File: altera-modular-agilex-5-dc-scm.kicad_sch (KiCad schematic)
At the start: 6 parts

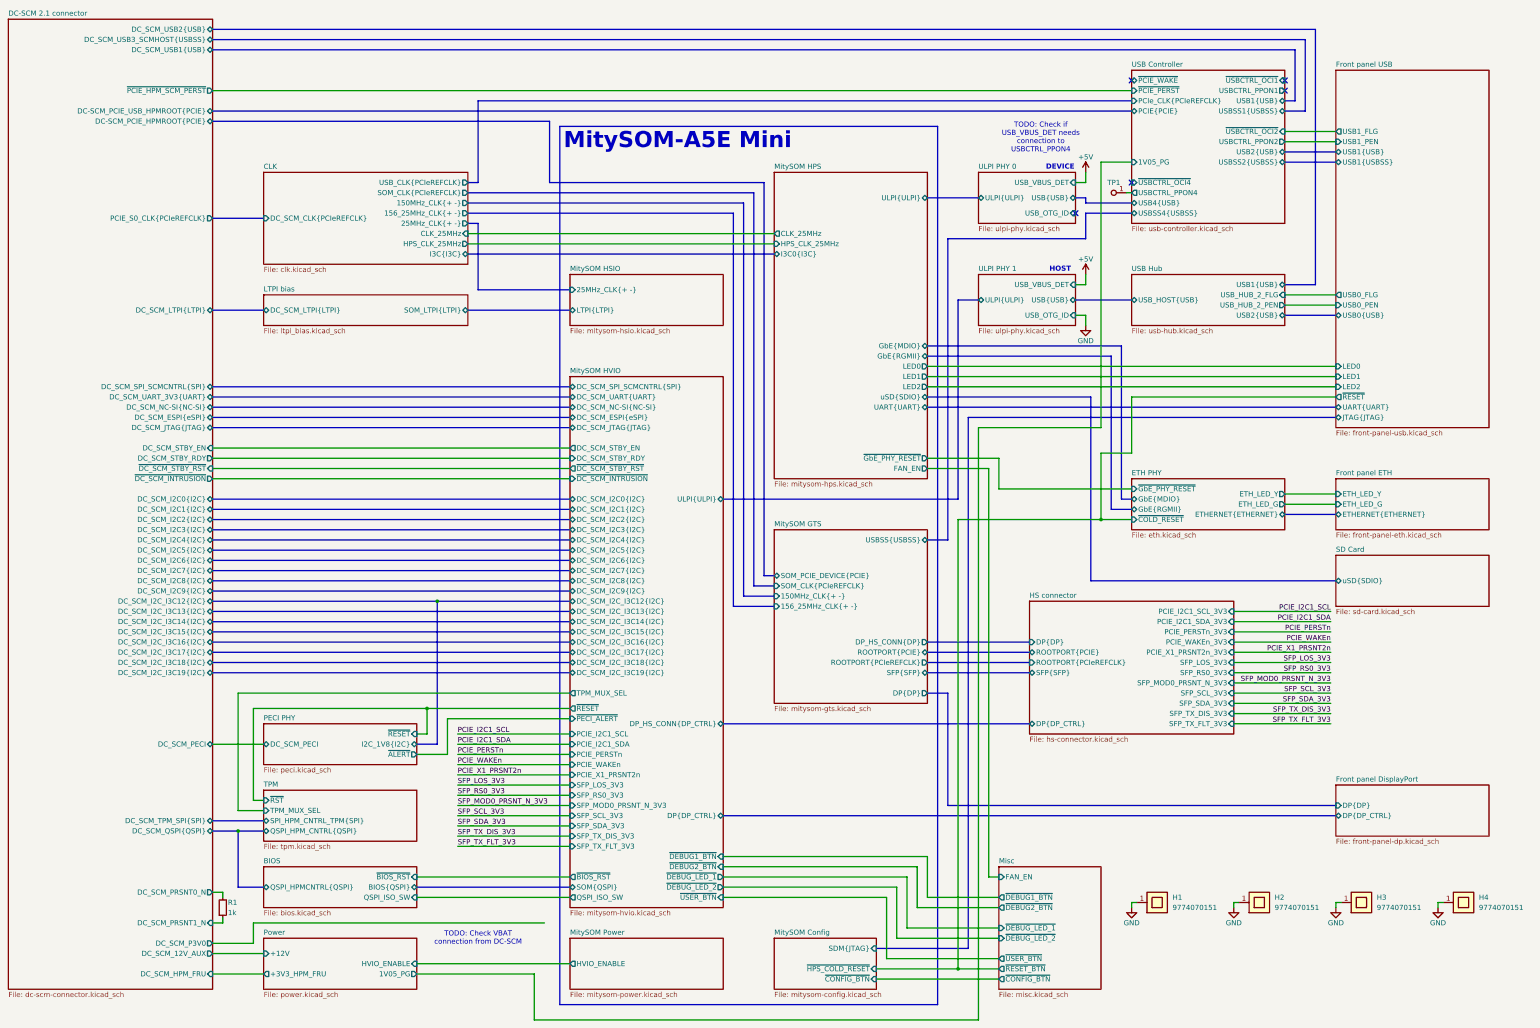
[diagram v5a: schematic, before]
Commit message: [#100595] Update connections according to client request
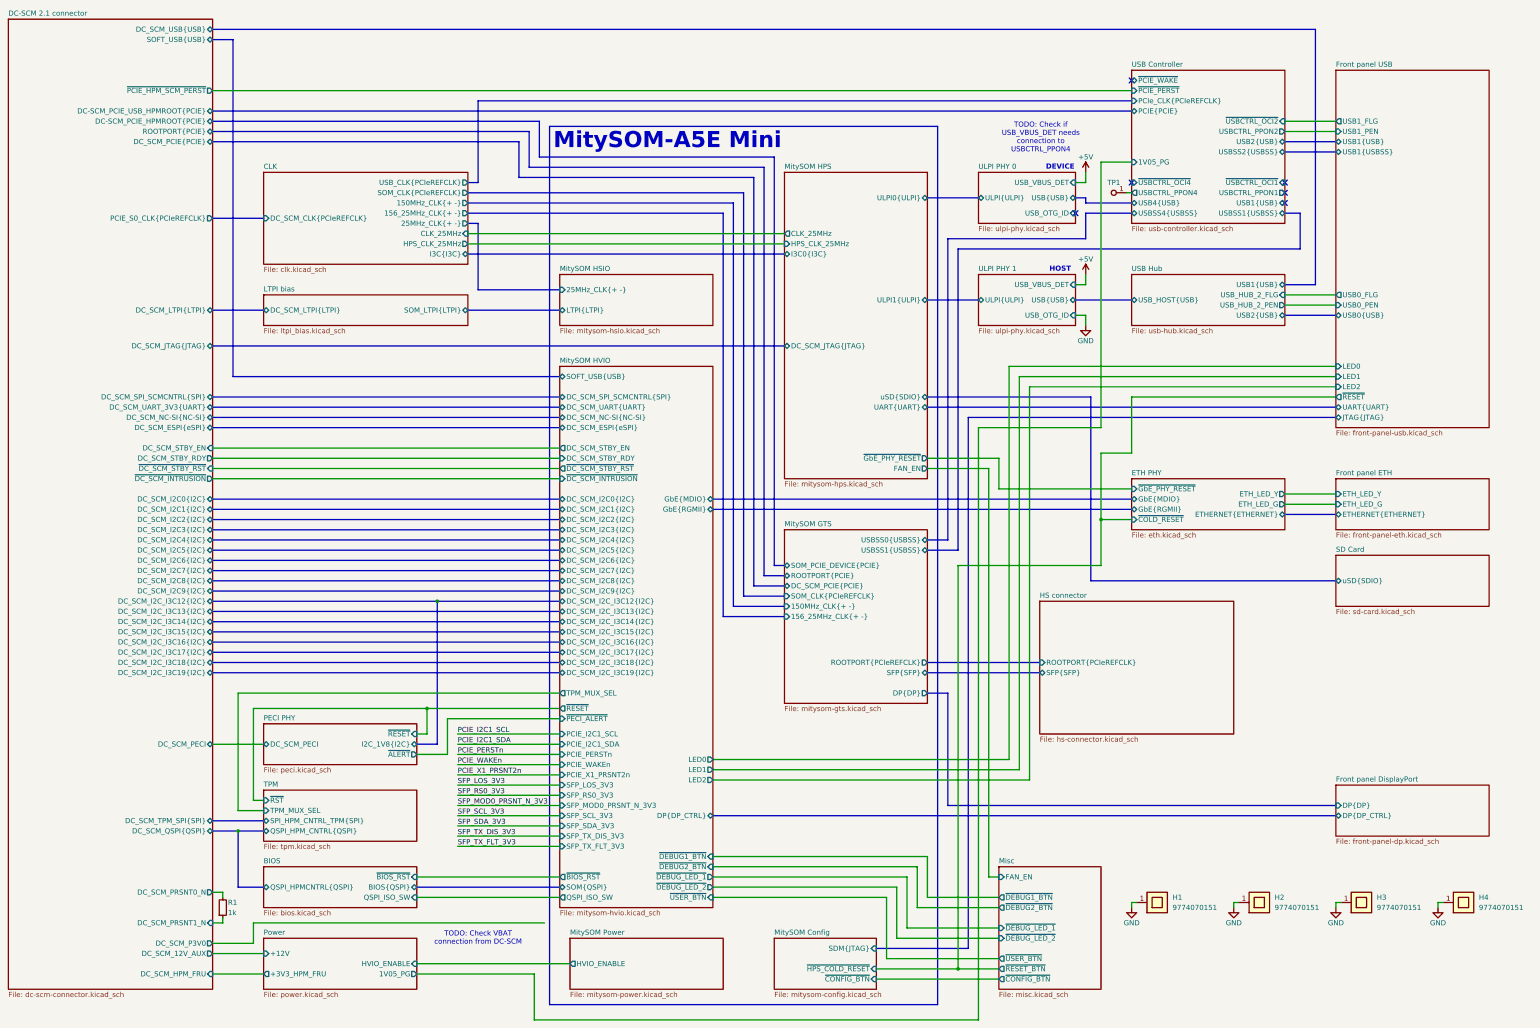
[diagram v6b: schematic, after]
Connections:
- no-connect marks 5 -> 6
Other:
- sheet DC-SCM 2.1 connector ports: added DC_SCM_PCIE{PCIE}, DC_SCM_USB{USB}, ROOTPORT{PCIE}, SOFT_USB{USB}; removed DC_SCM_USB1{USB}, DC_SCM_USB2{USB}, DC_SCM_USB3_SCMHOST{USBSS}
- sheet HS connector ports: added none; removed DP{DP_CTRL}, DP{DP}, PCIE_I2C1_SCL_3V3, PCIE_I2C1_SDA_3V3, PCIE_PERSTn_3V3, PCIE_WAKEn_3V3, PCIE_X1_PRSNT2n_3V3, ROOTPORT{PCIE}, SFP_LOS_3V3, SFP_MOD0_PRSNT_N_3V3, SFP_RS0_3V3, SFP_SCL_3V3, SFP_SDA_3V3, SFP_TX_DIS_3V3, SFP_TX_FLT_3V3
- sheet MitySOM GTS ports: added DC_SCM_PCIE{PCIE}, USBSS0{USBSS}, USBSS1{USBSS}; removed DP_HS_CONN{DP}, USBSS{USBSS}
- sheet MitySOM HPS ports: added DC_SCM_JTAG{JTAG}, ULPI0{ULPI}, ULPI1{ULPI}; removed GbE{MDIO}, GbE{RGMII}, LED0, LED1, LED2, ULPI{ULPI}
- sheet MitySOM HVIO ports: added GbE{MDIO}, GbE{RGMII}, LED0, LED1, LED2, SOFT_USB{USB}; removed DC_SCM_JTAG{JTAG}, DP_HS_CONN{DP_CTRL}, ULPI{ULPI}

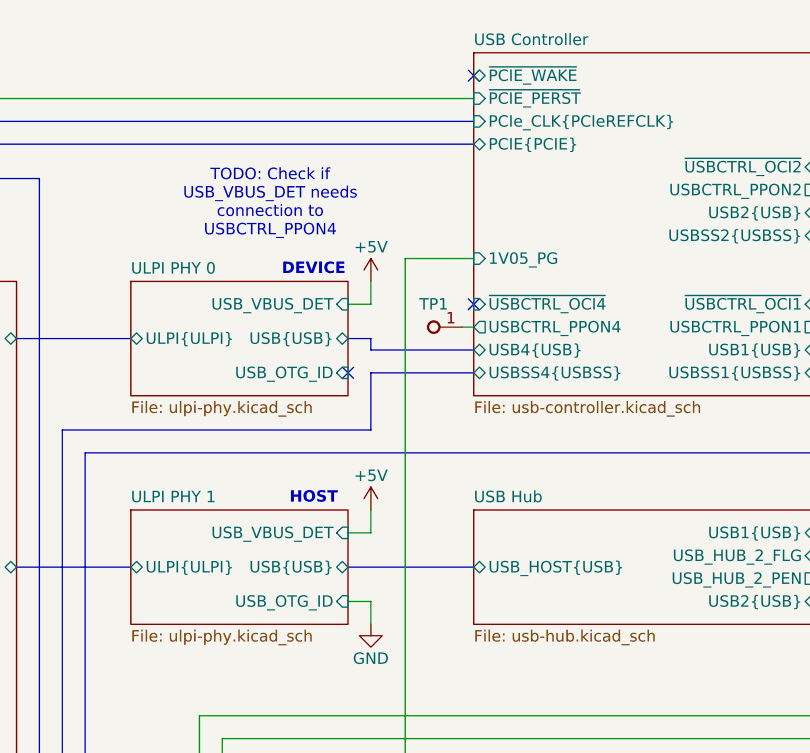
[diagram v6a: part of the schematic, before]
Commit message: [#100501] Connect ULPI CPEN signal to USB hub VBUS_DET
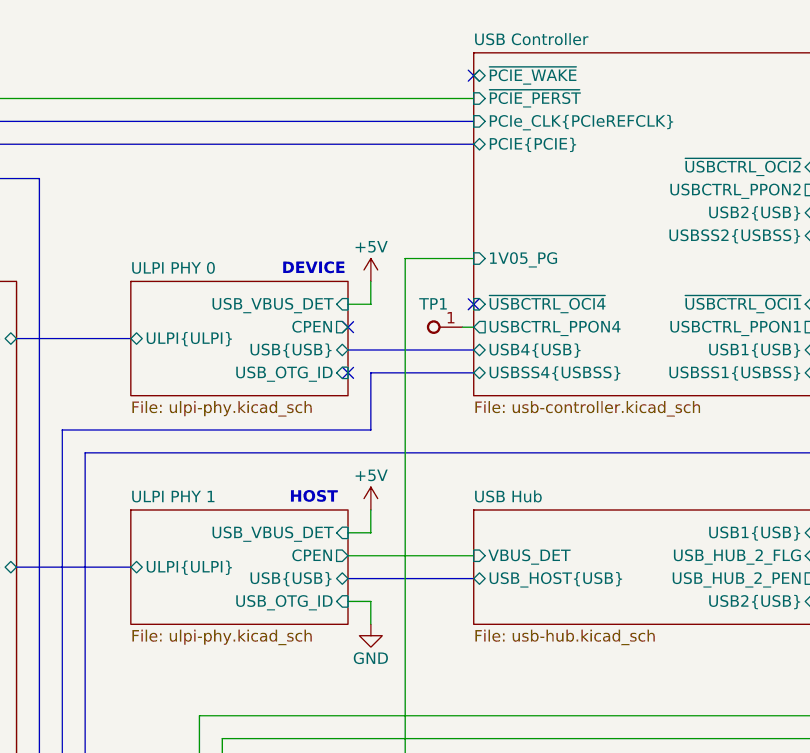
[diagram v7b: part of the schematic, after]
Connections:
- no-connect marks 6 -> 7
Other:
- sheet ULPI PHY 0 ports: added CPEN; removed none
- sheet ULPI PHY 1 ports: added CPEN; removed none
- sheet USB Hub ports: added VBUS_DET; removed none
- note removed: "TODO: Check if USB_VBUS_DET needs connection to USBCTRL_PPON4"
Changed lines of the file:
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@@
 		(company "Altera")
 	)
-	(text "TODO: Check if\nUSB_VBUS_DET needs\nconnection to\nUSBCTRL_PPON4"
-		(exclude_from_sim no)
-		(at 282.194 54.864 0)
-		(effects
-			(font
-				(size 1.27 1.27)
-			)
-		)
-	)
 	(text "HOST"
 		(exclude_from_sim no)
@@
 	)
 	(no_connect
+		(at 290.83 68.58)
+	)
+	(no_connect
 		(at 304.8 40.64)
 	)
@@
 	(bus
 		(pts
-			(xy 290.83 69.85) (xy 293.37 69.85)
+			(xy 290.83 71.12) (xy 304.8 71.12)
 		)
 		(stroke
@@
 	(wire
 		(pts
+			(xy 290.83 93.98) (xy 304.8 93.98)
+		)
+		(stroke
+			(width 0)
+			(type default)
+		)
+	)
+	(wire
+		(pts
 			(xy 261.62 261.62) (xy 271.78 261.62)
 		)
@@
 	(bus
 		(pts
-			(xy 304.8 71.12) (xy 293.37 71.12)
-		)
-		(stroke
-			(width 0)
-			(type default)
-		)
-	)
-	(bus
-		(pts
-			(xy 290.83 95.25) (xy 304.8 95.25)
+			(xy 290.83 96.52) (xy 304.8 96.52)
 		)
 		(stroke
@@
 		)
 	)
-	(bus
-		(pts
-			(xy 293.37 71.12) (xy 293.37 69.85)
-		)
-		(stroke
-			(width 0)
-			(type default)
-		)
-	)
 	(wire
 		(pts
@@
 		)
 		(pin "USB_HOST{USB}" bidirectional
-			(at 304.8 95.25 180)
+			(at 304.8 96.52 180)
 			(effects
 				(font
@@
 			)
 		)
+		(pin "VBUS_DET" input
+			(at 304.8 93.98 180)
+			(effects
+				(font
+					(size 1.27 1.27)
+				)
+				(justify left)
+			)
+		)
 		(instances
 			(project "altera-modular-agilex-5-dc-scm"
@@
 		)
 		(pin "USB{USB}" bidirectional
-			(at 290.83 69.85 0)
+			(at 290.83 71.12 0)
+			(effects
+				(font
+					(size 1.27 1.27)
+				)
+				(justify right)
+			)
+		)
+		(pin "CPEN" output
+			(at 290.83 68.58 0)
 			(effects
 				(font
@@
 		)
 		(pin "USB{USB}" bidirectional
-			(at 290.83 95.25 0)
+			(at 290.83 96.52 0)
+			(effects
+				(font
+					(size 1.27 1.27)
+				)
+				(justify right)
+			)
+		)
+		(pin "CPEN" output
+			(at 290.83 93.98 0)
 			(effects
 				(font

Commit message: [#100595] Update HS connections
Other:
- sheet HS connector ports: added PCIE_CLKREQ_N, PCIE_DET_WAKE, PCIE_PWR_EN, PCIE_RST_B; removed none
- sheet MitySOM HVIO ports: added PCIE_CLKREQ_N, PCIE_DET_WAKE, PCIE_PWR_EN, PCIE_RST_B; removed PCIE_I2C1_SCL, PCIE_I2C1_SDA, PCIE_PERSTn, PCIE_WAKEn, PCIE_X1_PRSNT2n, SFP_LOS_3V3, SFP_MOD0_PRSNT_N_3V3, SFP_RS0_3V3, SFP_SCL_3V3, SFP_SDA_3V3, SFP_TX_DIS_3V3, SFP_TX_FLT_3V3
